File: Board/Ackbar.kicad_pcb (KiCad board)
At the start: 2 copper layers, 101.6 x 50.8 mm, 13 parts, among them J1 TOF, J2 GNSS, J3 HALL, J4 MOTOR, J5 PWR_IN, J6 EPD, U1 ESP32-S3 Pico, U2 VREG, U3 TMC2209

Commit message: Cleanup
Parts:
- U1: footprint Akbar:Waveshare ESP32-S3 Pico -> Ackbar:Waveshare ESP32-S3 Pico
- U2: footprint Akbar:Buck Regulator -> Ackbar:Buck Regulator
- U3: footprint Akbar:BTT TMC2209 -> Ackbar:BTT TMC2209
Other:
- board text added: "Ackbar v0.2"
- board text removed: "Akbar v0.2"
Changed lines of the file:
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@@
   (net 39 "/M_B1")
   (net 40 "/M_B2")
-  (footprint "Akbar:Waveshare ESP32-S3 Pico" (layer "F.Cu")
+  (footprint "Ackbar:Waveshare ESP32-S3 Pico" (layer "F.Cu")
     (at 48.938 38.654334)
-    (property "Sheetfile" "Akbar.kicad_sch")
+    (property "Sheetfile" "Ackbar.kicad_sch")
     (property "Sheetname" "")
     (attr through_hole)
@@
   (footprint "SparkFun-Connector:1X05" (layer "F.Cu")
     (at 27.348 17.064334)
-    (property "Sheetfile" "Akbar.kicad_sch")
+    (property "Sheetfile" "Ackbar.kicad_sch")
     (property "Sheetname" "")
     (property "ki_description" "Generic connector, single row, 01x05, script generated (kicad-library-utils/schlib/autogen/connector/)")
@@
   (footprint "SparkFun-Connector:1X05" (layer "F.Cu")
     (at 45.128 17.064334)
-    (property "Sheetfile" "Akbar.kicad_sch")
+    (property "Sheetfile" "Ackbar.kicad_sch")
     (property "Sheetname" "")
     (property "ki_description" "Generic connector, single row, 01x05, script generated (kicad-library-utils/schlib/autogen/connector/)")
@@
   (footprint "SparkFun-Connector:1X04" (layer "F.Cu")
     (at 81.915 17.145)
-    (property "Sheetfile" "Akbar.kicad_sch")
+    (property "Sheetfile" "Ackbar.kicad_sch")
     (property "Sheetname" "")
     (property "ki_description" "Generic connector, single row, 01x04, script generated (kicad-library-utils/schlib/autogen/connector/)")
@@
       (net 40 "/M_B2") (pinfunction "Pin_4") (pintype "passive") (solder_mask_margin 0.1016))
   )
-  (footprint "Akbar:Buck Regulator" (layer "F.Cu")
+  (footprint "Ackbar:Buck Regulator" (layer "F.Cu")
     (at 94.658 47.544334 180)
-    (property "Sheetfile" "Akbar.kicad_sch")
+    (property "Sheetfile" "Ackbar.kicad_sch")
     (property "Sheetname" "")
     (attr through_hole)
@@
   (footprint "SparkFun-Connector:1X03" (layer "F.Cu")
     (at 62.908 17.064334)
-    (property "Sheetfile" "Akbar.kicad_sch")
+    (property "Sheetfile" "Ackbar.kicad_sch")
     (property "Sheetname" "")
     (property "ki_description" "Generic connector, single row, 01x03, script generated (kicad-library-utils/schlib/autogen/connector/)")
@@
     (descr "Terminal Block 4Ucon ItemNo. 19963, 2 pins, pitch 3.5mm, size 7.7x7mm^2, drill diamater 1.2mm, pad diameter 2.4mm, see http://www.4uconnector.com/online/object/4udrawing/19963.pdf, script-generated using https://github.com/pointhi/kicad-footprint-generator/scripts/TerminalBlock_4Ucon")
     (tags "THT Terminal Block 4Ucon ItemNo. 19963 pitch 3.5mm size 7.7x7mm^2 drill 1.2mm pad 2.4mm")
-    (property "Sheetfile" "Akbar.kicad_sch")
+    (property "Sheetfile" "Ackbar.kicad_sch")
     (property "Sheetname" "")
     (property "ki_description" "Generic screw terminal, single row, 01x02, script generated (kicad-library-utils/schlib/autogen/connector/)")
@@
   (footprint "SparkFun-Connector:1X08" (layer "F.Cu")
     (at 27.348 57.704334)
-    (property "Sheetfile" "Akbar.kicad_sch")
+    (property "Sheetfile" "Ackbar.kicad_sch")
     (property "Sheetname" "")
     (property "ki_description" "Generic connector, single row, 01x08, script generated (kicad-library-utils/schlib/autogen/connector/)")
@@
     (pad "1" connect circle (at 0 0) (size 5.7 5.7) (layers "B.Cu" "B.Mask"))
   )
-  (footprint "Akbar:BTT TMC2209" (layer "F.Cu")
+  (footprint "Ackbar:BTT TMC2209" (layer "F.Cu")
     (at 85.768 33.574334)
-    (property "Sheetfile" "Akbar.kicad_sch")
+    (property "Sheetfile" "Ackbar.kicad_sch")
     (property "Sheetname" "")
     (attr through_hole)
@@
     (effects (font (size 1 1) (thickness 0.15)) (justify left bottom))
   )
-  (gr_text "Akbar v0.2" (at 18.458 47.544334 90) (layer "F.SilkS")
+  (gr_text "Ackbar v0.2" (at 18.458 47.544334 90) (layer "F.SilkS")
     (effects (font (size 2.54 2.54) (thickness 0.15)) (justify left bottom))
   )

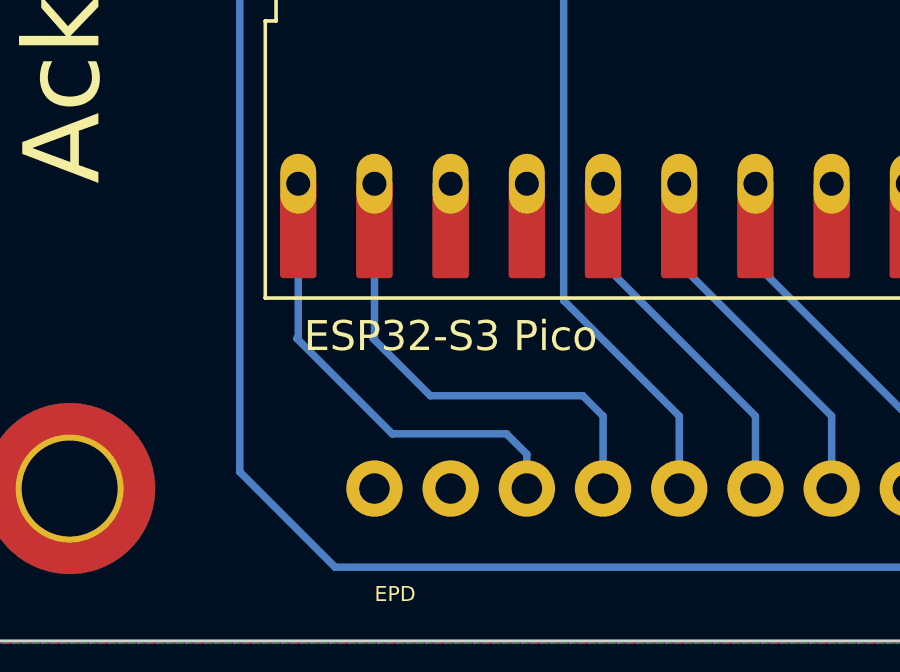
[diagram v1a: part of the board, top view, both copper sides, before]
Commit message: Cleanup ground fill
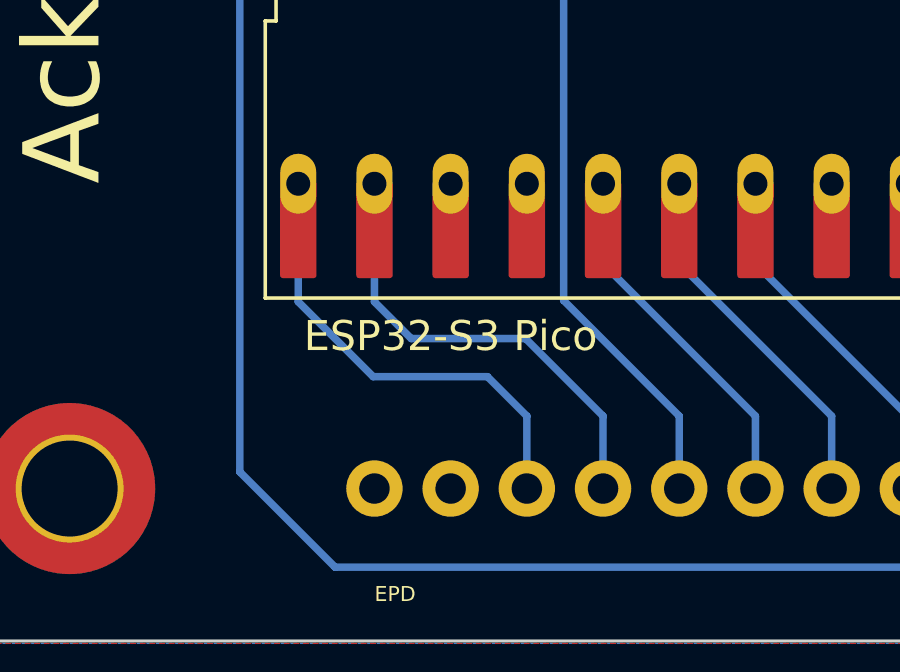
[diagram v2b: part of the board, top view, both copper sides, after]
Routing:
- net /SCK: track 16.3 -> 15.5 mm
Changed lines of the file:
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@@
   (segment (start 55.288 24.087) (end 55.288 17.064334) (width 0.25) (layer "B.Cu") (net 23))
   (segment (start 52.748 26.627) (end 55.288 24.087) (width 0.25) (layer "B.Cu") (net 23))
-  (segment (start 24.765 52.705) (end 24.808 52.662) (width 0.25) (layer "B.Cu") (net 24))
-  (segment (start 31.75 55.88) (end 27.94 55.88) (width 0.25) (layer "B.Cu") (net 24))
-  (segment (start 27.94 55.88) (end 24.765 52.705) (width 0.25) (layer "B.Cu") (net 24))
-  (segment (start 32.428 56.558) (end 31.75 55.88) (width 0.25) (layer "B.Cu") (net 24))
-  (segment (start 24.808 52.662) (end 24.808 47.544334) (width 0.25) (layer "B.Cu") (net 24))
-  (segment (start 32.428 57.704334) (end 32.428 56.558) (width 0.25) (layer "B.Cu") (net 24))
-  (segment (start 27.305 52.705) (end 27.348 52.662) (width 0.25) (layer "B.Cu") (net 25))
-  (segment (start 29.21 54.61) (end 27.305 52.705) (width 0.25) (layer "B.Cu") (net 25))
-  (segment (start 34.968 55.288) (end 34.29 54.61) (width 0.25) (layer "B.Cu") (net 25))
-  (segment (start 34.29 54.61) (end 29.21 54.61) (width 0.25) (layer "B.Cu") (net 25))
+  (segment (start 32.428 55.288) (end 31.115 53.975) (width 0.25) (layer "B.Cu") (net 24))
+  (segment (start 32.428 57.704334) (end 32.428 55.288) (width 0.25) (layer "B.Cu") (net 24))
+  (segment (start 31.115 53.975) (end 27.305 53.975) (width 0.25) (layer "B.Cu") (net 24))
+  (segment (start 24.808 51.478) (end 24.808 47.544334) (width 0.25) (layer "B.Cu") (net 24))
+  (segment (start 27.305 53.975) (end 24.808 51.478) (width 0.25) (layer "B.Cu") (net 24))
+  (segment (start 27.348 51.478) (end 27.348 47.544334) (width 0.25) (layer "B.Cu") (net 25))
+  (segment (start 32.385 52.705) (end 28.575 52.705) (width 0.25) (layer "B.Cu") (net 25))
+  (segment (start 28.575 52.705) (end 27.348 51.478) (width 0.25) (layer "B.Cu") (net 25))
   (segment (start 34.968 57.704334) (end 34.968 55.288) (width 0.25) (layer "B.Cu") (net 25))
-  (segment (start 27.348 52.662) (end 27.348 47.544334) (width 0.25) (layer "B.Cu") (net 25))
+  (segment (start 34.968 55.288) (end 32.385 52.705) (width 0.25) (layer "B.Cu") (net 25))
   (segment (start 37.508 57.704334) (end 37.508 55.288) (width 0.25) (layer "B.Cu") (net 26))
   (segment (start 37.508 55.288) (end 33.655 51.435) (width 0.25) (layer "B.Cu") (net 26))
